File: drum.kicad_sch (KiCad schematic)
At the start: 39 parts, among them J101 Cortex, J102 DX07S016JA3, SW101 SKSG, SW102 SKSG, U101 TPS78433QWDRBRQ1, U102 ATSAMD51J, Y101 32k768

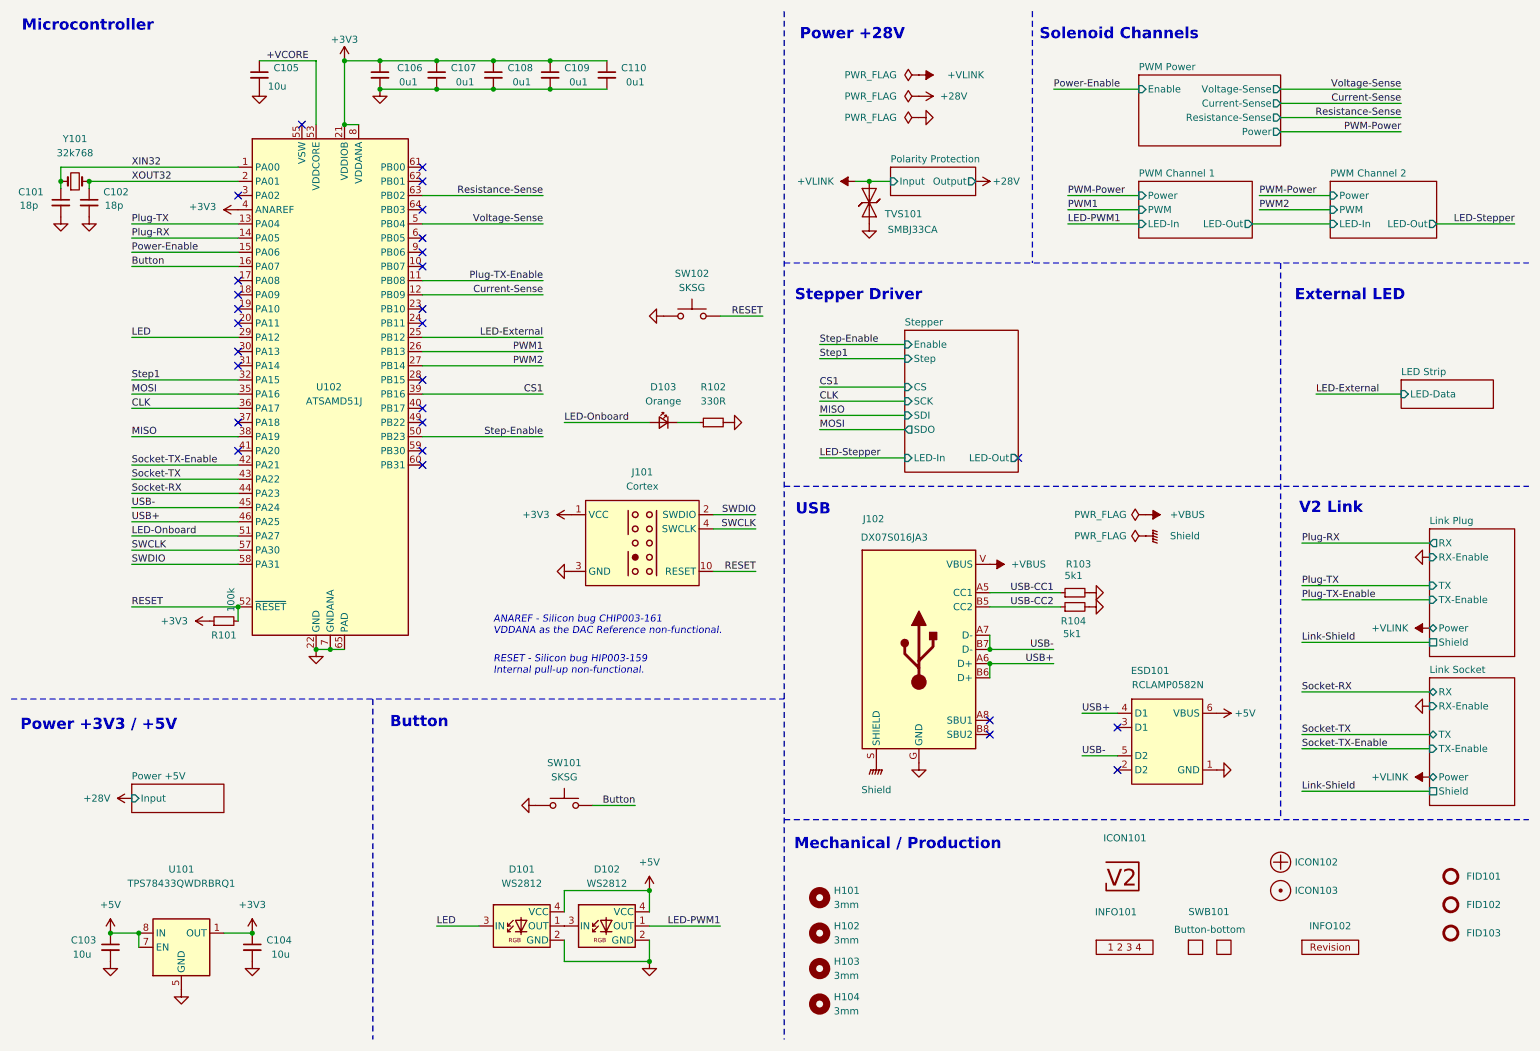
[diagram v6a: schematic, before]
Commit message: Switch to 6 layer
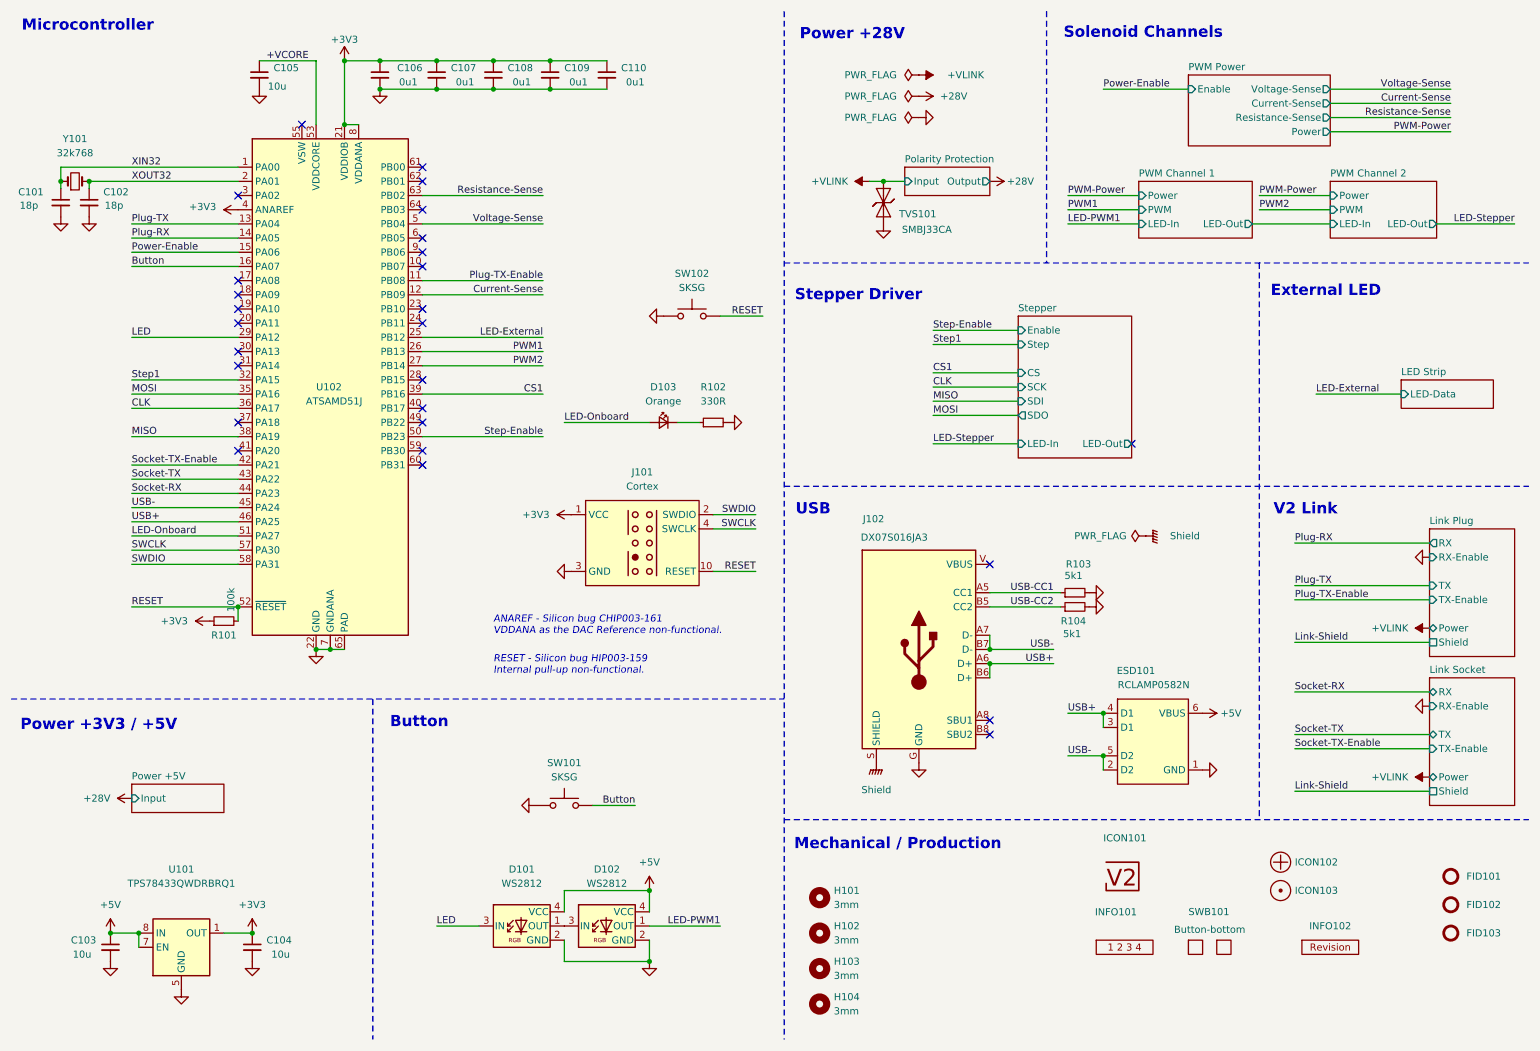
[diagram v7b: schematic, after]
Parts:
- INFO101: value Layer_Numbers -> Layer_Numbers-6; footprint V2_Production:Layer_Numbers -> V2_Production:Layer_Numbers-6; symbol V2_Production:Layer_Numbers -> V2_Production:Layer_Numbers-6
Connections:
- net USB+: now also ESD101.3 (D1)
- net USB-: now also ESD101.2 (D2)
- net +VBUS: no longer names the net of J102.V (VBUS)
- no-connect marks 28 -> 27
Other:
- moved on the sheet: ESD101, TVS101
